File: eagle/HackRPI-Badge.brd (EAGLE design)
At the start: 124.5 x 94 mm, 42 parts, among them J1 FTDI_BASICPTH, J2 SOLDERJUMPERTRACE-PTH, U2 3.3V, U4 74595, U5 74595, U6 74595, U7 74165DT, U8 AT25SF041

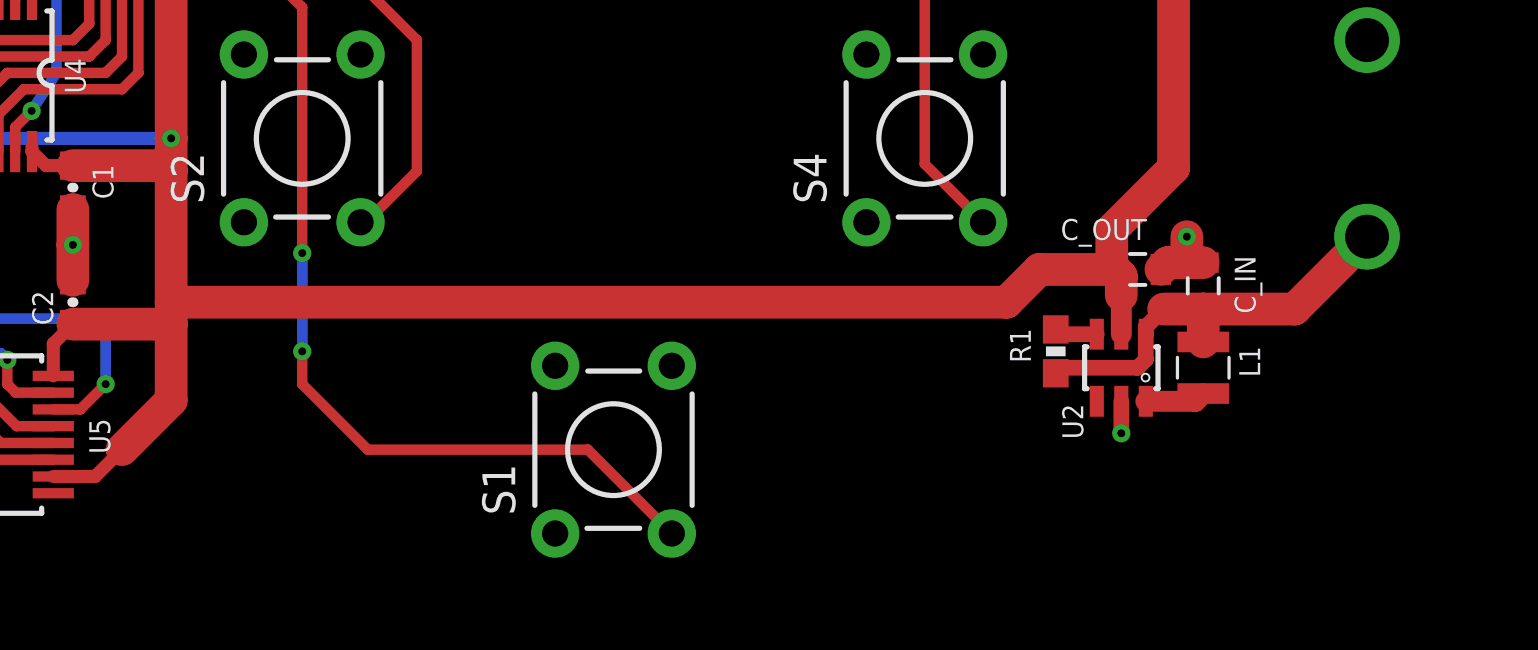
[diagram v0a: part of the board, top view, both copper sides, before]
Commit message: Fixed AAT1217 pinout and modified board for correct pinout
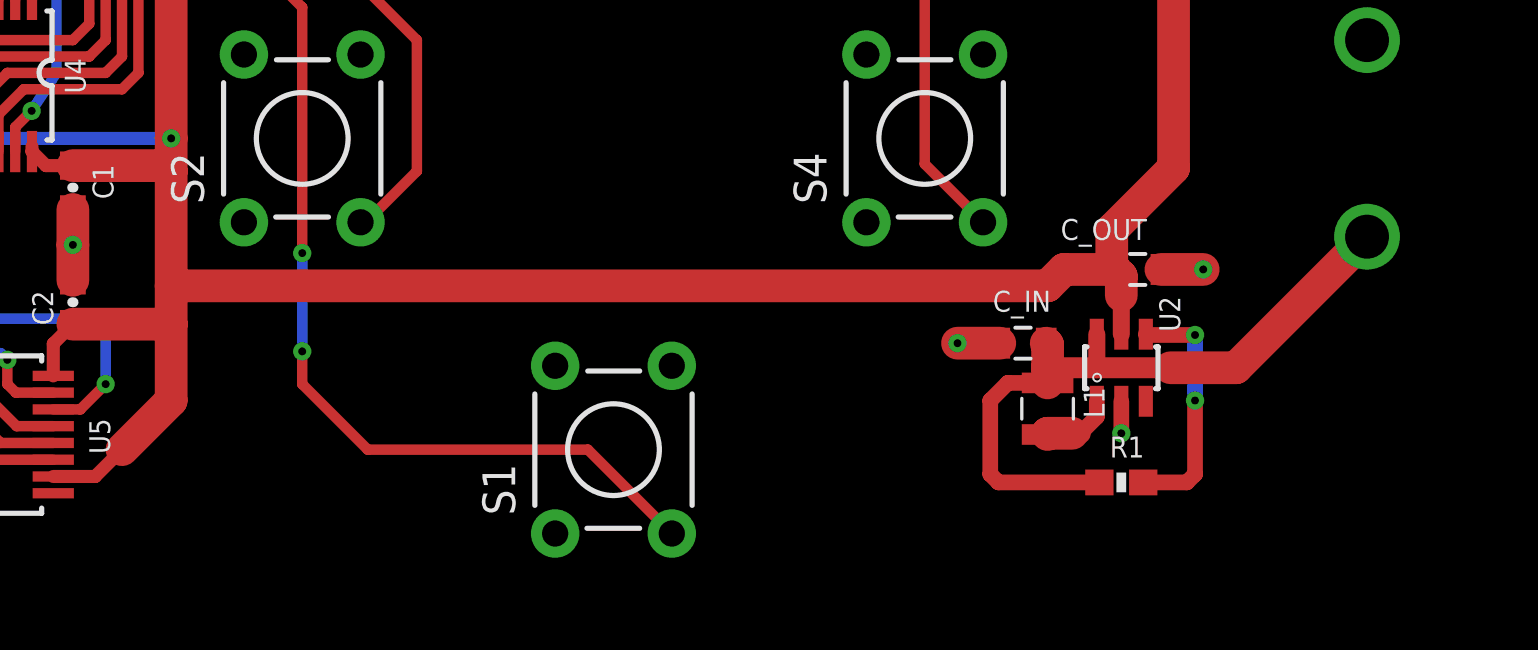
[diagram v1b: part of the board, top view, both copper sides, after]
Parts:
- moved C_IN 7.33 mm to (94.6, 20.0), turned to 180 degrees
- moved L1 6.24 mm to (95.6, 17.5)
- moved R1 5.68 mm to (98.4, 14.6), turned to 180 degrees
- turned U2 to 180 degrees
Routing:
- net V_BATT: track 16.3 -> 27.1 mm
- net N$6: track 1.67 -> 9.46 mm, vias 0 -> 2
- net GND: track 38.4 -> 38.3 mm, vias 14 -> 15

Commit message: Fixed ESP12 pinout
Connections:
- net LAT: now also U1.13; no longer U1.14
- net OE: now also U1.14; no longer U1.13
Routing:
- net OE: track 129.2 -> 127.4 mm
- net LAT: track 156.5 -> 155.7 mm
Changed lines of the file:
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@@
 <contactref element="U5" pad="12"/>
 <contactref element="U6" pad="12"/>
-<contactref element="U1" pad="14"/>
+<contactref element="U1" pad="13"/>
 <wire x1="53.6" y1="27.43" x2="53.6" y2="17.52" width="0.4064" layer="1"/>
 <wire x1="53.6" y1="17.52" x2="54.985" y2="16.135" width="0.4064" layer="1"/>
@@
 <wire x1="93.345" y1="73.66" x2="97.79" y2="78.105" width="0.4064" layer="1"/>
 <wire x1="97.79" y1="78.105" x2="98.425" y2="78.105" width="0.4064" layer="1"/>
-<wire x1="104.775" y1="78.105" x2="110.49" y2="78.105" width="0.508" layer="1"/>
-<wire x1="110.49" y1="78.105" x2="113.53" y2="81.145" width="0.508" layer="1"/>
-<wire x1="113.53" y1="81.145" x2="115.45" y2="81.145" width="0.508" layer="1"/>
+<wire x1="106.3625" y1="78.105" x2="111.76" y2="78.105" width="0.508" layer="1"/>
 <via x="98.425" y="78.105" extent="1-16" drill="0.3048"/>
-<wire x1="98.425" y1="78.105" x2="104.775" y2="78.105" width="0.508" layer="16"/>
-<via x="104.775" y="78.105" extent="1-16" drill="0.3048"/>
+<wire x1="98.425" y1="78.105" x2="106.3625" y2="78.105" width="0.508" layer="16"/>
+<via x="106.3625" y="78.105" extent="1-16" drill="0.3048"/>
 <wire x1="53.6" y1="27.43" x2="53.6" y2="30.105" width="0.4064" layer="1"/>
 <wire x1="53.6" y1="30.105" x2="54.61" y2="31.115" width="0.4064" layer="1"/>
@@
 <wire x1="49.8475" y1="71.755" x2="53.975" y2="67.6275" width="0.4064" layer="16"/>
 <wire x1="53.975" y1="67.6275" x2="53.975" y2="60.96" width="0.4064" layer="16"/>
+<wire x1="111.76" y1="78.105" x2="112.8" y2="79.145" width="0.508" layer="1"/>
+<wire x1="112.8" y1="79.145" x2="115.45" y2="79.145" width="0.508" layer="1"/>
 </signal>
 <signal name="OE">
@@
 <contactref element="U5" pad="13"/>
 <contactref element="U4" pad="13"/>
-<contactref element="U1" pad="13"/>
+<contactref element="U1" pad="14"/>
 <wire x1="54.25" y1="27.43" x2="54.25" y2="18.14" width="0.4064" layer="1"/>
 <wire x1="54.25" y1="18.14" x2="55.605" y2="16.785" width="0.4064" layer="1"/>
@@
 <via x="97.155" y="78.74" extent="1-16" drill="0.3048"/>
 <wire x1="97.155" y1="78.74" x2="98.425" y2="80.01" width="0.4064" layer="16"/>
-<wire x1="98.425" y1="80.01" x2="104.775" y2="80.01" width="0.508" layer="16"/>
-<wire x1="104.775" y1="80.01" x2="107.95" y2="76.835" width="0.508" layer="16"/>
-<via x="107.95" y="76.835" extent="1-16" drill="0.3048"/>
-<wire x1="107.95" y1="76.835" x2="111.125" y2="76.835" width="0.508" layer="1"/>
-<wire x1="111.125" y1="76.835" x2="113.435" y2="79.145" width="0.508" layer="1"/>
-<wire x1="113.435" y1="79.145" x2="115.45" y2="79.145" width="0.508" layer="1"/>
+<wire x1="98.425" y1="80.01" x2="106.3625" y2="80.01" width="0.508" layer="16"/>
+<via x="106.3625" y="80.01" extent="1-16" drill="0.3048"/>
+<wire x1="106.3625" y1="80.01" x2="111.76" y2="80.01" width="0.508" layer="1"/>
 <wire x1="54.25" y1="27.43" x2="54.25" y2="29.485" width="0.4064" layer="1"/>
 <wire x1="54.25" y1="29.485" x2="55.245" y2="30.48" width="0.4064" layer="1"/>
@@
 <wire x1="54.9275" y1="62.865" x2="55.2875" y2="62.505" width="0.4064" layer="1"/>
 <wire x1="55.2875" y1="62.505" x2="57.025" y2="62.505" width="0.4064" layer="1"/>
+<wire x1="111.76" y1="80.01" x2="112.895" y2="81.145" width="0.508" layer="1"/>
+<wire x1="112.895" y1="81.145" x2="115.45" y2="81.145" width="0.508" layer="1"/>
 </signal>
 <signal name="GPIO15">

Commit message: Fixed layout to use correct esp8266 pinout
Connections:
- net LAT: now also U1.14; no longer U1.13
- net OE: now also U1.13; no longer U1.14
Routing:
- net OE: track 127.4 -> 129.2 mm
- net LAT: track 155.7 -> 156.5 mm
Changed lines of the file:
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@@
 <contactref element="U5" pad="12"/>
 <contactref element="U6" pad="12"/>
-<contactref element="U1" pad="13"/>
+<contactref element="U1" pad="14"/>
 <wire x1="53.6" y1="27.43" x2="53.6" y2="17.52" width="0.4064" layer="1"/>
 <wire x1="53.6" y1="17.52" x2="54.985" y2="16.135" width="0.4064" layer="1"/>
@@
 <wire x1="93.345" y1="73.66" x2="97.79" y2="78.105" width="0.4064" layer="1"/>
 <wire x1="97.79" y1="78.105" x2="98.425" y2="78.105" width="0.4064" layer="1"/>
-<wire x1="106.3625" y1="78.105" x2="111.76" y2="78.105" width="0.508" layer="1"/>
+<wire x1="104.775" y1="78.105" x2="110.49" y2="78.105" width="0.508" layer="1"/>
+<wire x1="110.49" y1="78.105" x2="113.53" y2="81.145" width="0.508" layer="1"/>
+<wire x1="113.53" y1="81.145" x2="115.45" y2="81.145" width="0.508" layer="1"/>
 <via x="98.425" y="78.105" extent="1-16" drill="0.3048"/>
-<wire x1="98.425" y1="78.105" x2="106.3625" y2="78.105" width="0.508" layer="16"/>
-<via x="106.3625" y="78.105" extent="1-16" drill="0.3048"/>
+<wire x1="98.425" y1="78.105" x2="104.775" y2="78.105" width="0.508" layer="16"/>
+<via x="104.775" y="78.105" extent="1-16" drill="0.3048"/>
 <wire x1="53.6" y1="27.43" x2="53.6" y2="30.105" width="0.4064" layer="1"/>
 <wire x1="53.6" y1="30.105" x2="54.61" y2="31.115" width="0.4064" layer="1"/>
@@
 <wire x1="49.8475" y1="71.755" x2="53.975" y2="67.6275" width="0.4064" layer="16"/>
 <wire x1="53.975" y1="67.6275" x2="53.975" y2="60.96" width="0.4064" layer="16"/>
-<wire x1="111.76" y1="78.105" x2="112.8" y2="79.145" width="0.508" layer="1"/>
-<wire x1="112.8" y1="79.145" x2="115.45" y2="79.145" width="0.508" layer="1"/>
 </signal>
 <signal name="OE">
@@
 <contactref element="U5" pad="13"/>
 <contactref element="U4" pad="13"/>
-<contactref element="U1" pad="14"/>
+<contactref element="U1" pad="13"/>
 <wire x1="54.25" y1="27.43" x2="54.25" y2="18.14" width="0.4064" layer="1"/>
 <wire x1="54.25" y1="18.14" x2="55.605" y2="16.785" width="0.4064" layer="1"/>
@@
 <via x="97.155" y="78.74" extent="1-16" drill="0.3048"/>
 <wire x1="97.155" y1="78.74" x2="98.425" y2="80.01" width="0.4064" layer="16"/>
-<wire x1="98.425" y1="80.01" x2="106.3625" y2="80.01" width="0.508" layer="16"/>
-<via x="106.3625" y="80.01" extent="1-16" drill="0.3048"/>
-<wire x1="106.3625" y1="80.01" x2="111.76" y2="80.01" width="0.508" layer="1"/>
+<wire x1="98.425" y1="80.01" x2="104.775" y2="80.01" width="0.508" layer="16"/>
+<wire x1="104.775" y1="80.01" x2="107.95" y2="76.835" width="0.508" layer="16"/>
+<via x="107.95" y="76.835" extent="1-16" drill="0.3048"/>
+<wire x1="107.95" y1="76.835" x2="111.125" y2="76.835" width="0.508" layer="1"/>
+<wire x1="111.125" y1="76.835" x2="113.435" y2="79.145" width="0.508" layer="1"/>
+<wire x1="113.435" y1="79.145" x2="115.45" y2="79.145" width="0.508" layer="1"/>
 <wire x1="54.25" y1="27.43" x2="54.25" y2="29.485" width="0.4064" layer="1"/>
 <wire x1="54.25" y1="29.485" x2="55.245" y2="30.48" width="0.4064" layer="1"/>
@@
 <wire x1="54.9275" y1="62.865" x2="55.2875" y2="62.505" width="0.4064" layer="1"/>
 <wire x1="55.2875" y1="62.505" x2="57.025" y2="62.505" width="0.4064" layer="1"/>
-<wire x1="111.76" y1="80.01" x2="112.895" y2="81.145" width="0.508" layer="1"/>
-<wire x1="112.895" y1="81.145" x2="115.45" y2="81.145" width="0.508" layer="1"/>
 </signal>
 <signal name="GPIO15">

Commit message: Tented vias, added HackRPI logo on back of board
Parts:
- added U$1: (no value), mylib:HACKRPI-LOGO
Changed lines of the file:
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@@
 <attribute name="PARTNO" value="AT25SF041-SSHD-T" x="91.44" y="54.61" size="1.778" layer="27" rot="R90" display="off"/>
 </element>
+<element name="U$1" library="mylib" package="HACKRPI-LOGO" value="" x="60.325" y="46.6725" rot="MR270"/>
 </elements>
 <signals>

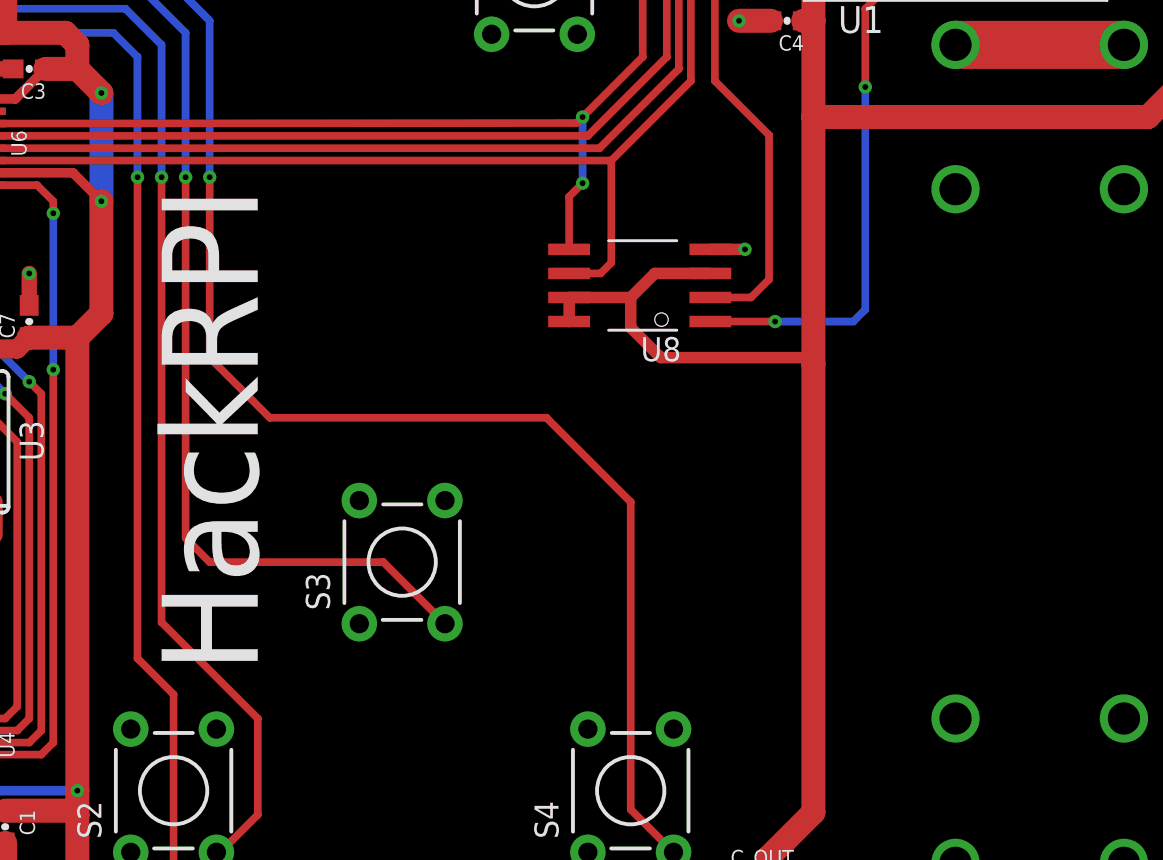
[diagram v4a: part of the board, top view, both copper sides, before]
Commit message: Added HackRPI screw on front of board, removed temporary HackRPI text
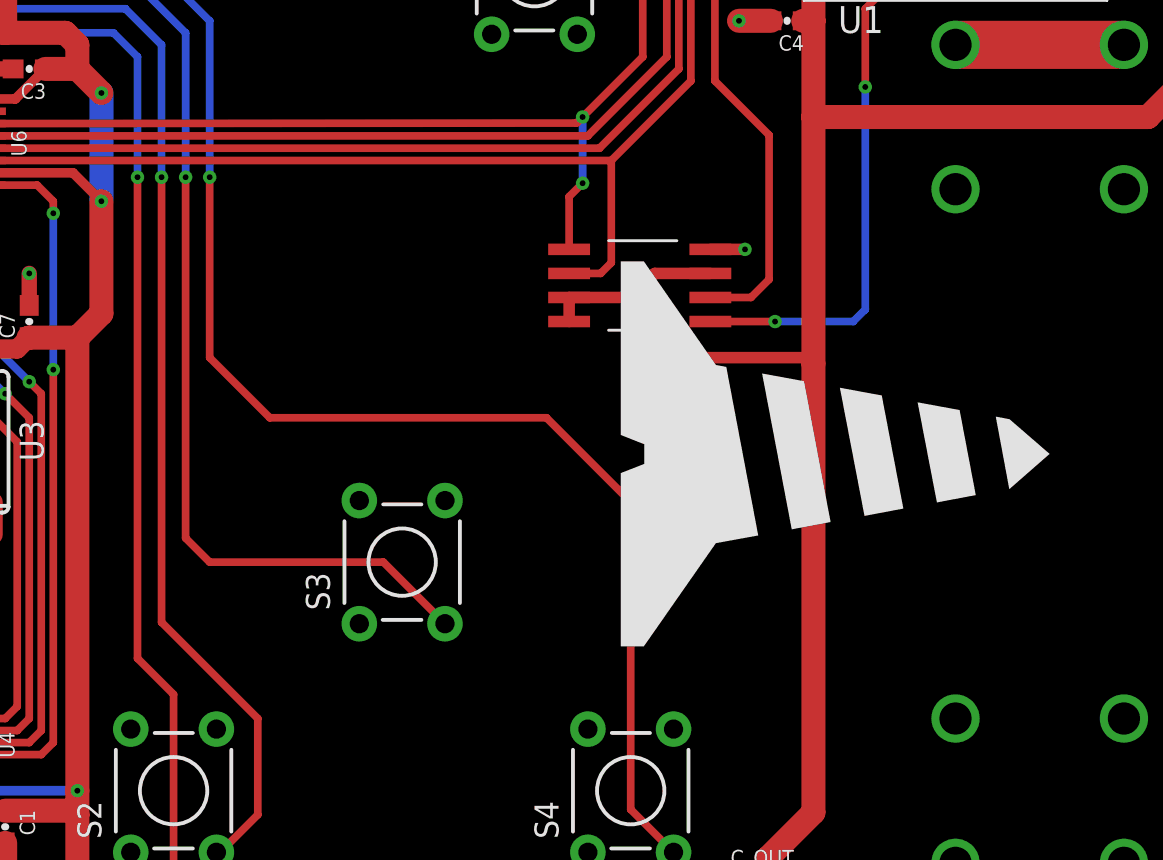
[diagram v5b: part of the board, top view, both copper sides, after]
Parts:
- added U$2: (no value), mylib:HACKRPI-SCREW
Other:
- board text removed: "HackRPI"
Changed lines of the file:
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@@
 <wire x1="3.81" y1="50.8" x2="7.62" y2="50.8" width="0" layer="20" curve="-180"/>
 <wire x1="7.62" y1="41.91" x2="3.81" y2="41.91" width="0" layer="20" curve="-180"/>
-<text x="68.58" y="46.99" size="5.08" layer="21" rot="R90" align="center">HackRPI</text>
 <text x="120.65" y="3.81" size="2.54" layer="21" rot="R180" align="top-left">Prototype Batch 1</text>
 </plain>
@@
 <param name="mlMinCreamFrame" value="0mil"/>
 <param name="mlMaxCreamFrame" value="0mil"/>
-<param name="mlViaStopLimit" value="0mil"/>
+<param name="mlViaStopLimit" value="15mil"/>
 <param name="srRoundness" value="0"/>
 <param name="srMinRoundness" value="0mil"/>
@@
 </element>
 <element name="U$1" library="mylib" package="HACKRPI-LOGO" value="" x="60.325" y="46.6725" rot="MR270"/>
+<element name="U$2" library="mylib" package="HACKRPI-SCREW" value="" x="101.6" y="45.72" rot="R90"/>
 </elements>
 <signals>
